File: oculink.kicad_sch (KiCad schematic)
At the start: 18 parts, among them J9 OCuLink_x4_Amphenol_G14A42121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

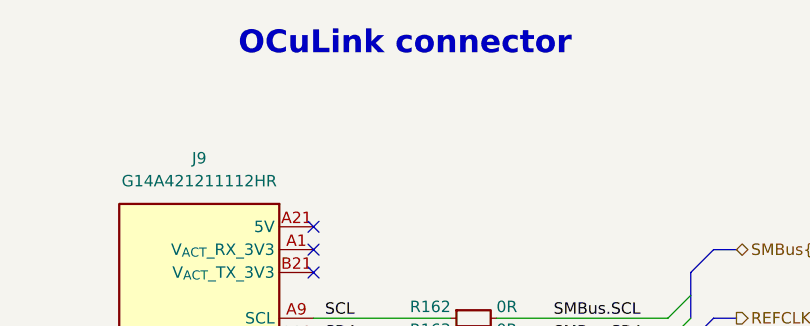
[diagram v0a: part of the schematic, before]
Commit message: [#86617] Unify captions, add TVS to USB VBUS
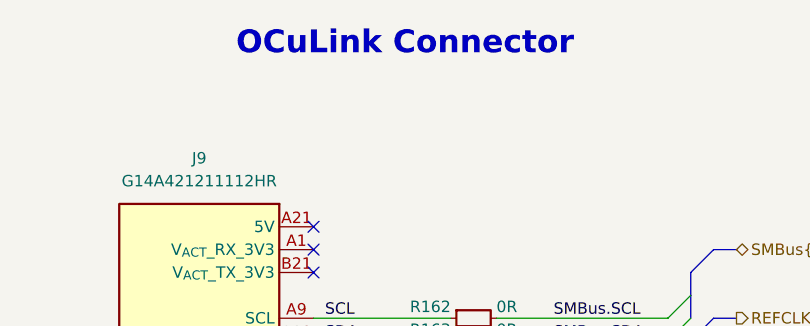
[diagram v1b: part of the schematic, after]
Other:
- note added: "OCuLink Connector"
- note removed: "OCuLink connector"
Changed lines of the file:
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@@
 		(comment 1 "www.antmicro.com")
 	)
-	(text "OCuLink connector"
+	(text "OCuLink Connector"
 		(exclude_from_sim no)
 		(at 201.93 64.77 0)

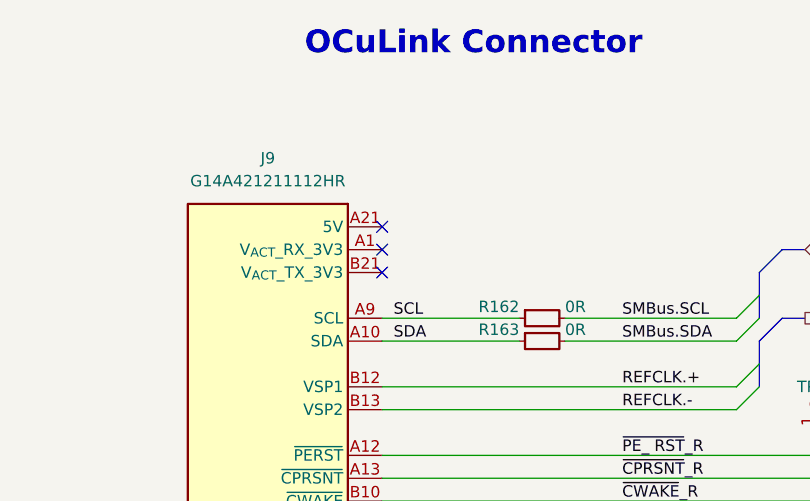
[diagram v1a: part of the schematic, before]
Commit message: [#86617] Power U10 from OCuLink, remove JTAG sheet pin, fix I2C cross
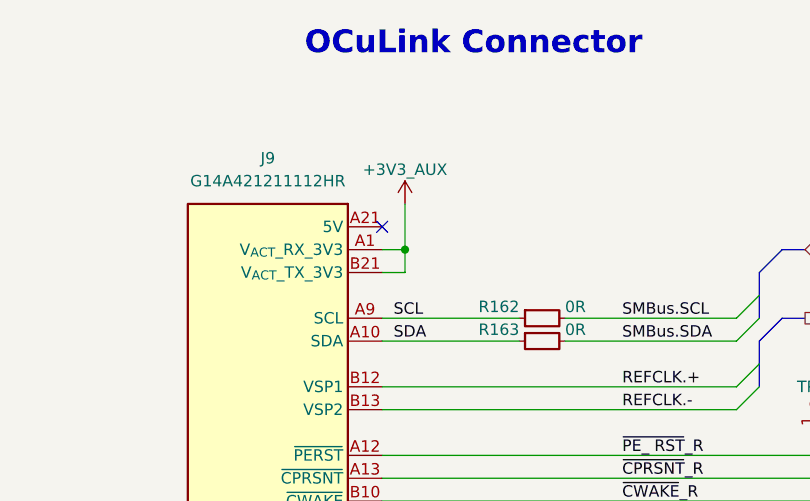
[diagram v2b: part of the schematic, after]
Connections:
- net +3V3_AUX: now reaches J9.A1 (V_{ACT}_RX_3V3)
- net +3V3_AUX: now also J9.B21 (V_{ACT}_TX_3V3)
- no-connect marks 4 -> 2
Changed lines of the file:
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@@
 	)
 	(junction
+		(at 194.31 87.63)
+		(diameter 0)
+		(color 0 0 0 0)
+	)
+	(junction
 		(at 257.81 110.49)
 		(diameter 0)
@@
 	)
 	(no_connect
-		(at 191.77 87.63)
-	)
-	(no_connect
-		(at 191.77 90.17)
-	)
-	(no_connect
 		(at 261.62 214.63)
 	)
@@
 	(wire
 		(pts
+			(xy 191.77 90.17) (xy 194.31 90.17)
+		)
+		(stroke
+			(width 0)
+			(type default)
+		)
+	)
+	(wire
+		(pts
 			(xy 275.59 105.41) (xy 275.59 115.57)
 		)
@@
 	(wire
 		(pts
+			(xy 191.77 87.63) (xy 194.31 87.63)
+		)
+		(stroke
+			(width 0)
+			(type default)
+		)
+	)
+	(wire
+		(pts
 			(xy 245.11 113.03) (xy 266.7 113.03)
 		)
@@
 	(wire
 		(pts
+			(xy 194.31 87.63) (xy 194.31 82.55)
+		)
+		(stroke
+			(width 0)
+			(type default)
+		)
+	)
+	(wire
+		(pts
 			(xy 261.62 242.57) (xy 246.38 242.57)
 		)
@@
 		)
 	)
+	(wire
+		(pts
+			(xy 194.31 90.17) (xy 194.31 87.63)
+		)
+		(stroke
+			(width 0)
+			(type default)
+		)
+	)
 	(bus
 		(pts
@@
 					(unit 1)
 				)
+			)
+		)
+	)
+	(symbol
+		(lib_id "antmicropower:+3V3_AON")
+		(at 194.31 82.55 0)
+		(unit 1)
+		(exclude_from_sim no)
+		(in_bom yes)
+		(on_board yes)
+		(dnp no)
+		(property "Reference" "#PWR099"
+			(at 194.31 86.36 0)
+			(effects
+				(font
+					(size 1.27 1.27)
+				)
+				(hide yes)
+			)
+		)
+		(property "Value" "+3V3_AUX"
+			(at 194.31 78.74 0)
+			(effects
+				(font
+					(size 1.27 1.27)
+				)
+			)
+		)
+		(property "Footprint" ""
+			(at 194.31 82.55 0)
+			(effects
+				(font
+					(size 1.27 1.27)
+				)
+				(hide yes)
+			)
+		)
+		(property "Datasheet" ""
+			(at 194.31 82.55 0)
+			(effects
+				(font
+					(size 1.27 1.27)
+				)
+				(hide yes)
+			)
+		)
+		(property "Description" ""
+			(at 194.31 88.9 0)
+			(effects
+				(font
+					(size 1.27 1.27)
+				)
+				(justify left bottom)
+				(hide yes)
+			)
+		)
+		(pin "1"
+		)
+		(instances
+			(project ""
+				(path "/04bda987-e5eb-48b4-9e90-d8211dc11b39/0cbe4665-19ed-43d5-9283-363c2bb680b6"
+					(reference "#PWR099")
+					(unit 1)
+				)

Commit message: [#86351] Rename project
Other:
- title: 10GbE Expansion -> OCuLink to 10GbE adapter
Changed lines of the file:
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@@
 	(paper "A3")
 	(title_block
-		(title "10GbE Expansion")
+		(title "OCuLink to 10GbE adapter")
 		(date "2025-11-07")
 		(rev "1.0.0")
@@
 		)
 		(instances
-			(project "10-gbe-expansion"
+			(project "OCuLink to 10GbE adapter"
 				(path "/04bda987-e5eb-48b4-9e90-d8211dc11b39/0cbe4665-19ed-43d5-9283-363c2bb680b6"
 					(reference "R166")
@@
 		)
 		(instances
-			(project "10-gbe-expansion"
+			(project "OCuLink to 10GbE adapter"
 				(path "/04bda987-e5eb-48b4-9e90-d8211dc11b39/0cbe4665-19ed-43d5-9283-363c2bb680b6"
 					(reference "D8")
@@
 		)
 		(instances
-			(project "10-gbe-expansion"
+			(project "OCuLink to 10GbE adapter"
 				(path "/04bda987-e5eb-48b4-9e90-d8211dc11b39/0cbe4665-19ed-43d5-9283-363c2bb680b6"
 					(reference "R162")
@@
 		)
 		(instances
-			(project "10-gbe-expansion"
+			(project "OCuLink to 10GbE adapter"
 				(path "/04bda987-e5eb-48b4-9e90-d8211dc11b39/0cbe4665-19ed-43d5-9283-363c2bb680b6"
 					(reference "D9")
@@
 		)
 		(instances
-			(project "10-gbe-expansion"
+			(project "OCuLink to 10GbE adapter"
 				(path "/04bda987-e5eb-48b4-9e90-d8211dc11b39/0cbe4665-19ed-43d5-9283-363c2bb680b6"
 					(reference "#PWR0322")
@@
 		)
 		(instances
-			(project "10-gbe-expansion"
+			(project "OCuLink to 10GbE adapter"
 				(path "/04bda987-e5eb-48b4-9e90-d8211dc11b39/0cbe4665-19ed-43d5-9283-363c2bb680b6"
 					(reference "D4")
@@
 		)
 		(instances
-			(project "10-gbe-expansion"
+			(project "OCuLink to 10GbE adapter"
 				(path "/04bda987-e5eb-48b4-9e90-d8211dc11b39/0cbe4665-19ed-43d5-9283-363c2bb680b6"
 					(reference "#PWR0324")
@@
 		)
 		(instances
-			(project "10-gbe-expansion"
+			(project "OCuLink to 10GbE adapter"
 				(path "/04bda987-e5eb-48b4-9e90-d8211dc11b39/0cbe4665-19ed-43d5-9283-363c2bb680b6"
 					(reference "D6")
@@
 		)
 		(instances
-			(project "10-gbe-expansion"
+			(project "OCuLink to 10GbE adapter"
 				(path "/04bda987-e5eb-48b4-9e90-d8211dc11b39/0cbe4665-19ed-43d5-9283-363c2bb680b6"
 					(reference "#PWR0321")
@@
 		)
 		(instances
-			(project "10-gbe-expansion"
+			(project "OCuLink to 10GbE adapter"
 				(path "/04bda987-e5eb-48b4-9e90-d8211dc11b39/0cbe4665-19ed-43d5-9283-363c2bb680b6"
 					(reference "R163")
@@
 		)
 		(instances
-			(project "10-gbe-expansion"
+			(project "OCuLink to 10GbE adapter"
 				(path "/04bda987-e5eb-48b4-9e90-d8211dc11b39/0cbe4665-19ed-43d5-9283-363c2bb680b6"
 					(reference "R167")
@@
 		)
 		(instances
-			(project "10-gbe-expansion"
+			(project "OCuLink to 10GbE adapter"
 				(path "/04bda987-e5eb-48b4-9e90-d8211dc11b39/0cbe4665-19ed-43d5-9283-363c2bb680b6"
 					(reference "D5")
@@
 		)
 		(instances
-			(project "10-gbe-expansion"
+			(project "OCuLink to 10GbE adapter"
 				(path "/04bda987-e5eb-48b4-9e90-d8211dc11b39/0cbe4665-19ed-43d5-9283-363c2bb680b6"
 					(reference "#PWR0326")
@@
 		)
 		(instances
-			(project "10-gbe-expansion"
+			(project "OCuLink to 10GbE adapter"
 				(path "/04bda987-e5eb-48b4-9e90-d8211dc11b39/0cbe4665-19ed-43d5-9283-363c2bb680b6"
 					(reference "TP15")
@@
 		)
 		(instances
-			(project "10-gbe-expansion"
+			(project "OCuLink to 10GbE adapter"
 				(path "/04bda987-e5eb-48b4-9e90-d8211dc11b39/0cbe4665-19ed-43d5-9283-363c2bb680b6"
 					(reference "#PWR0327")
@@
 		)
 		(instances
-			(project "10-gbe-expansion"
+			(project "OCuLink to 10GbE adapter"
 				(path "/04bda987-e5eb-48b4-9e90-d8211dc11b39/0cbe4665-19ed-43d5-9283-363c2bb680b6"
 					(reference "R165")
@@
 		)
 		(instances
-			(project "10-gbe-expansion"
+			(project "OCuLink to 10GbE adapter"
 				(path "/04bda987-e5eb-48b4-9e90-d8211dc11b39/0cbe4665-19ed-43d5-9283-363c2bb680b6"
 					(reference "#PWR0323")
@@
 		)
 		(instances
-			(project "10-gbe-expansion"
+			(project "OCuLink to 10GbE adapter"
 				(path "/04bda987-e5eb-48b4-9e90-d8211dc11b39/0cbe4665-19ed-43d5-9283-363c2bb680b6"
 					(reference "#PWR0325")
@@
 		)
 		(instances
-			(project "10-gbe-expansion"
+			(project "OCuLink to 10GbE adapter"
 				(path "/04bda987-e5eb-48b4-9e90-d8211dc11b39/0cbe4665-19ed-43d5-9283-363c2bb680b6"
 					(reference "R168")
@@
 		)
 		(instances
-			(project "10-gbe-expansion"
+			(project "OCuLink to 10GbE adapter"
 				(path "/04bda987-e5eb-48b4-9e90-d8211dc11b39/0cbe4665-19ed-43d5-9283-363c2bb680b6"
 					(reference "TP16")

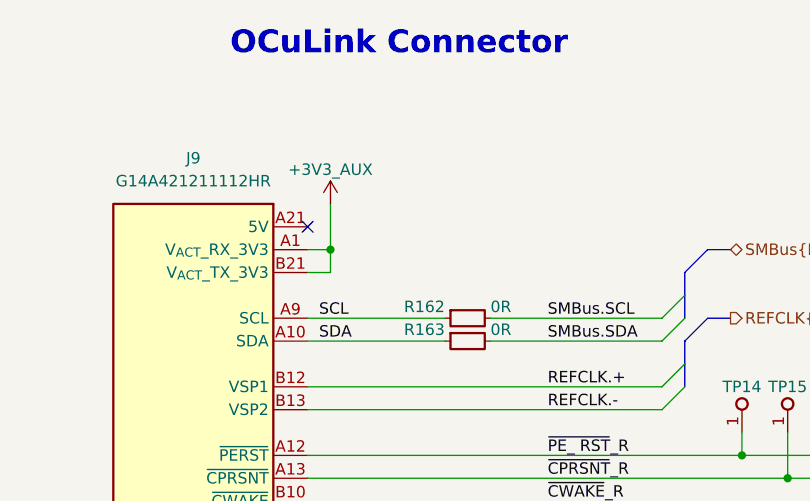
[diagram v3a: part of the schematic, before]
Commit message: [#86351] Connect Tag Connect 3V3 pin, clear ERC
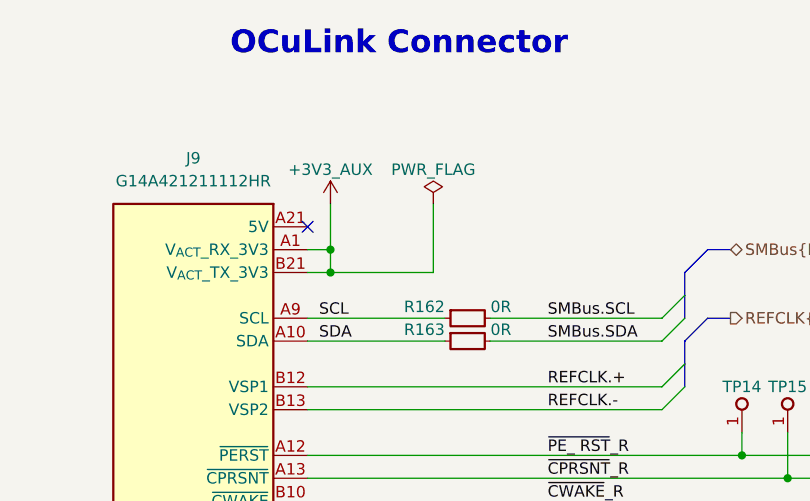
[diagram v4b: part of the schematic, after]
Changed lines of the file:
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@@
+	)
+	(junction
+		(at 194.31 90.17)
+		(diameter 0)
+		(color 0 0 0 0)
 	)
 	(junction
@@
 	(wire
 		(pts
-			(xy 194.31 87.63) (xy 194.31 82.55)
-		)
-		(stroke
-			(width 0)
-			(type default)
-		)
-	)
-	(wire
-		(pts
 			(xy 261.62 242.57) (xy 246.38 242.57)
 		)
@@
 	(wire
 		(pts
+			(xy 194.31 90.17) (xy 194.31 87.63)
+		)
+		(stroke
+			(width 0)
+			(type default)
+		)
+	)
+	(wire
+		(pts
 			(xy 191.77 135.89) (xy 231.14 135.89)
 		)
@@
 		)
 	)
-	(wire
-		(pts
-			(xy 194.31 90.17) (xy 194.31 87.63)
-		)
-		(stroke
-			(width 0)
-			(type default)
-		)
-	)
 	(bus
 		(pts
@@
 	(wire
 		(pts
+			(xy 205.74 90.17) (xy 205.74 82.55)
+		)
+		(stroke
+			(width 0)
+			(type default)
+		)
+	)
+	(wire
+		(pts
 			(xy 275.59 100.33) (xy 275.59 97.79)
 		)
@@
 	(wire
 		(pts
+			(xy 194.31 82.55) (xy 194.31 87.63)
+		)
+		(stroke
+			(width 0)
+			(type default)
+		)
+	)
+	(wire
+		(pts
 			(xy 191.77 158.75) (xy 231.14 158.75)
 		)
@@
 		(pts
 			(xy 259.08 245.11) (xy 259.08 247.65)
+		)
+		(stroke
+			(width 0)
+			(type default)
+		)
+	)
+	(wire
+		(pts
+			(xy 205.74 90.17) (xy 194.31 90.17)
 		)
 		(stroke
@@
 					(unit 1)
 				)
+			)
+		)
+	)
+	(symbol
+		(lib_id "antmicropower:PWR_FLAG")
+		(at 205.74 82.55 0)
+		(unit 1)
+		(exclude_from_sim no)
+		(in_bom yes)
+		(on_board yes)
+		(dnp no)
+		(property "Reference" "#FLG021"
+			(at 205.74 80.645 0)
+			(effects
+				(font
+					(size 1.27 1.27)
+				)
+				(hide yes)
+			)
+		)
+		(property "Value" "PWR_FLAG"
+			(at 205.74 78.74 0)
+			(effects
+				(font
+					(size 1.27 1.27)
+				)
+			)
+		)
+		(property "Footprint" ""
+			(at 205.74 82.55 0)
+			(effects
+				(font
+					(size 1.27 1.27)
+				)
+				(hide yes)
+			)
+		)
+		(property "Datasheet" ""
+			(at 205.74 82.55 0)
+			(effects
+				(font
+					(size 1.27 1.27)
+				)
+				(hide yes)
+			)
+		)
+		(property "Description" ""
+			(at 205.74 85.09 0)
+			(effects
+				(font
+					(size 1.27 1.27)
+				)
+				(justify left bottom)
+				(hide yes)
+			)
+		)
+		(pin "1"
+		)
+		(instances
+			(project ""
+				(path "/04bda987-e5eb-48b4-9e90-d8211dc11b39/0cbe4665-19ed-43d5-9283-363c2bb680b6"
+					(reference "#FLG021")
+					(unit 1)
+				)

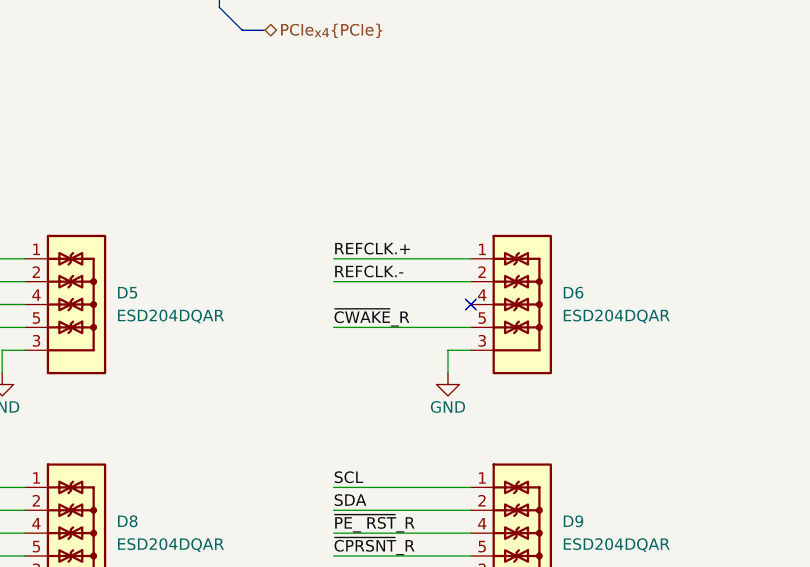
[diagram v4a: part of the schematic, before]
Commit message: [#86351] WIP: Passives component placement
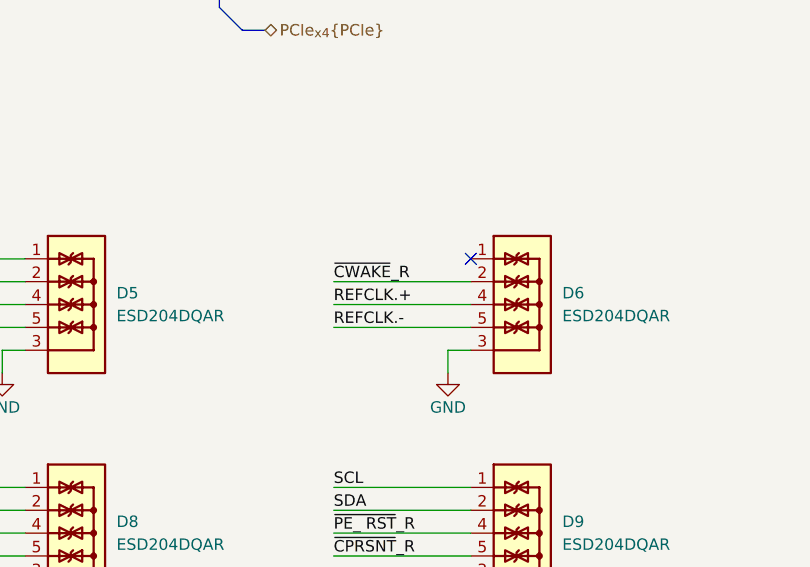
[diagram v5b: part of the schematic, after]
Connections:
- net REFCLK.+: now also D6.4, D6.7; no longer D6.1, D6.10
- net REFCLK.-: now also D6.5, D6.6; no longer D6.2, D6.9
- net ~{CWAKE}_R: now also D6.2, D6.9; no longer D6.5, D6.6
- new net: D6.1, D6.10
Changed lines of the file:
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@@
-	)
-	(no_connect
-		(at 261.62 214.63)
 	)
 	(no_connect
 		(at 191.77 85.09)
 	)
+	(no_connect
+		(at 261.62 209.55)
+	)
 	(bus_entry
 		(at 233.68 146.05)
@@
 	(wire
 		(pts
-			(xy 261.62 209.55) (xy 246.38 209.55)
-		)
-		(stroke
-			(width 0)
-			(type default)
-		)
-	)
-	(wire
-		(pts
 			(xy 158.75 219.71) (xy 158.75 222.25)
 		)
@@
 	(wire
 		(pts
+			(xy 246.38 212.09) (xy 261.62 212.09)
+		)
+		(stroke
+			(width 0)
+			(type default)
+		)
+	)
+	(wire
+		(pts
 			(xy 158.75 245.11) (xy 161.29 245.11)
 		)
@@
 	(wire
 		(pts
-			(xy 246.38 217.17) (xy 261.62 217.17)
-		)
-		(stroke
-			(width 0)
-			(type default)
-		)
-	)
-	(wire
-		(pts
 			(xy 261.62 240.03) (xy 246.38 240.03)
 		)
@@
 	(wire
 		(pts
+			(xy 261.62 214.63) (xy 246.38 214.63)
+		)
+		(stroke
+			(width 0)
+			(type default)
+		)
+	)
+	(wire
+		(pts
 			(xy 161.29 217.17) (xy 146.05 217.17)
 		)
@@
 	(wire
 		(pts
-			(xy 261.62 212.09) (xy 246.38 212.09)
-		)
-		(stroke
-			(width 0)
-			(type default)
-		)
-	)
-	(wire
-		(pts
 			(xy 240.03 110.49) (xy 257.81 110.49)
 		)
@@
 		(pts
 			(xy 259.08 245.11) (xy 261.62 245.11)
+		)
+		(stroke
+			(width 0)
+			(type default)
+		)
+	)
+	(wire
+		(pts
+			(xy 261.62 217.17) (xy 246.38 217.17)
 		)
 		(stroke
@@
 		)
 	)
+	(label "REFCLK.-"
+		(at 246.38 217.17 0)
+		(effects
+			(font
+				(size 1.27 1.27)
+			)
+			(justify left bottom)
+		)
+	)
 	(label "~{PE_ RST}_R"
 		(at 246.38 240.03 0)
@@
 		)
 	)
+	(label "~{CWAKE}_R"
+		(at 246.38 212.09 0)
+		(effects
+			(font
+				(size 1.27 1.27)
+			)
+			(justify left bottom)
+		)
+	)
 	(label "SMBus.SCL"
 		(at 218.44 95.25 0)
@@
 		)
 	)
-	(label "~{CWAKE}_R"
-		(at 246.38 217.17 0)
-		(effects
-			(font
-				(size 1.27 1.27)
-			)
-			(justify left bottom)
-		)
-	)
 	(label "PCIe_{x4}.RX1-"
 		(at 146.05 217.17 0)
@@
 		)
 	)
+	(label "REFCLK.+"
+		(at 246.38 214.63 0)
+		(effects
+			(font
+				(size 1.27 1.27)
+			)
+			(justify left bottom)
+		)
+	)
 	(label "PCIe_{x4}.TX2+"
 		(at 196.85 234.95 0)
@@
 		)
 	)
-	(label "REFCLK.-"
-		(at 246.38 212.09 0)
-		(effects
-			(font
-				(size 1.27 1.27)
-			)
-			(justify left bottom)
-		)
-	)
 	(label "PCIe_{x4}.TX3+"
 		(at 196.85 240.03 0)
@@
 		(effects
 			(font
-				(size 1.27 1.27)
-			)
-			(justify left bottom)
-		)
-	)
-	(label "REFCLK.+"
-		(at 246.38 209.55 0)
-		(effects
-			(font

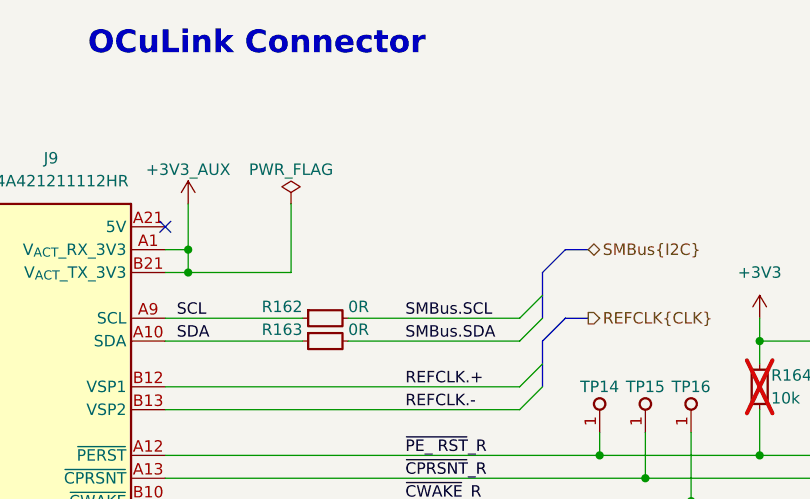
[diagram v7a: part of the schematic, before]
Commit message: [#89038] Add OCuLink 3V3 indicator LED, add polarity marking for DC connector
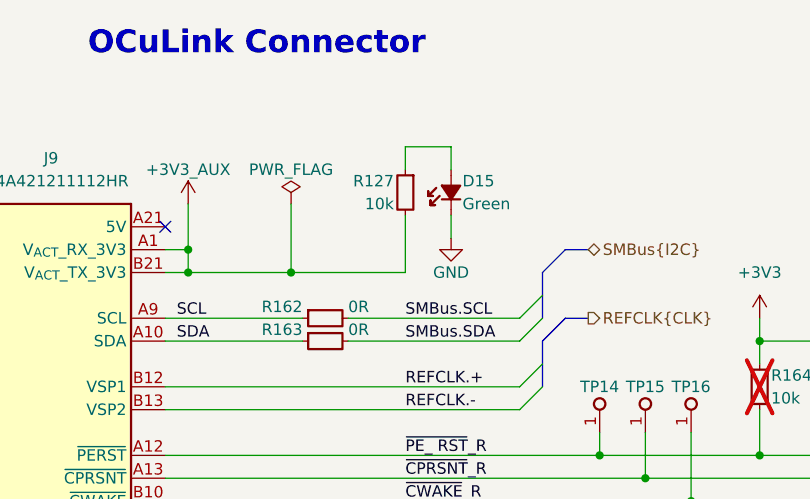
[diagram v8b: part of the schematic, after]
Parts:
- added D15: LED_G_0603_LG_L29K-G2J1-24-Z, antmicro-footprints:LED_0603_1608Metric_G, symbol antmicroLEDIndicationDiscrete:LED_G_0603_LG_L29K-G2J1-24-Z
- added R127: R_10k_0402, antmicro-footprints:R_0402_1005Metric, symbol antmicroResistors0402:R_10k_0402
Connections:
- net +3V3_AUX: now also R127.2
- net GND: now also D15.1 (C)
- new net: D15.2 (A), R127.1
